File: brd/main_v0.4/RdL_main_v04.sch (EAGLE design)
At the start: 22 parts, among them J1 Test, J2 MPU

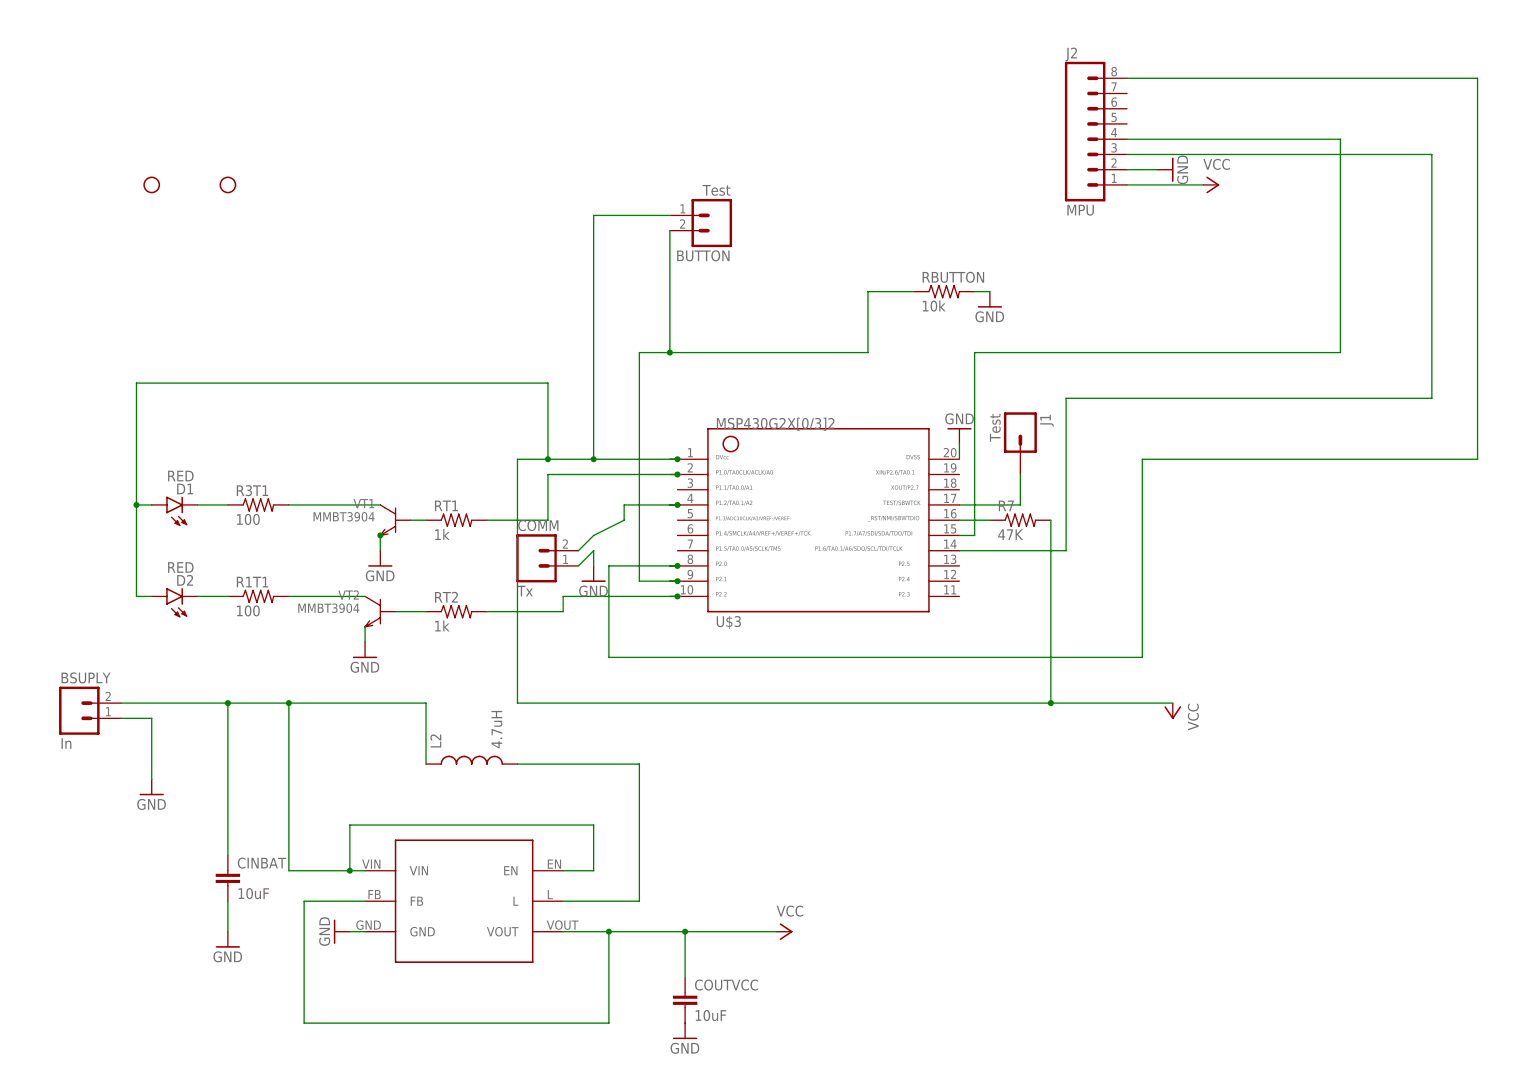
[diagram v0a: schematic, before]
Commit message: Added version 4 to divide in 3 boards
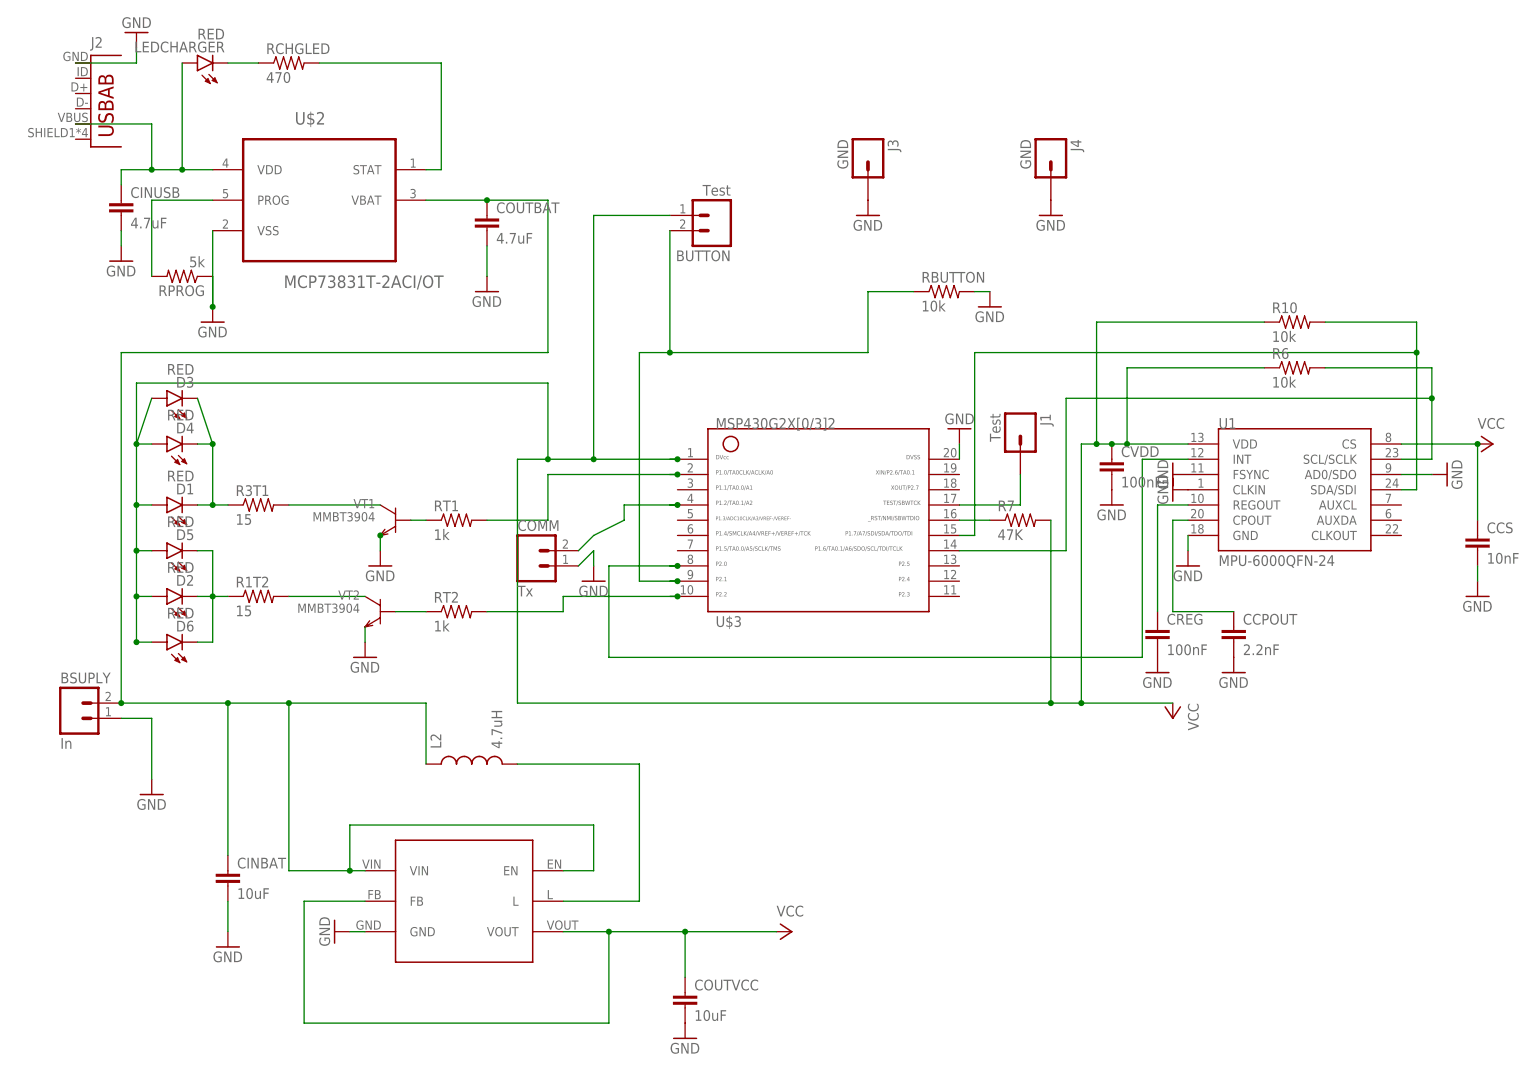
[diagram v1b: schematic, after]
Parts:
- removed H1, H3: STAND-OFF, SparkFun-Electromechanical:STAND-OFF
- added CCPOUT: 2.2nF, SparkFun-Capacitors:CAP0805
- added CCS: 10nF, SparkFun-Capacitors:CAP0805
- added CINUSB, COUTBAT: 4.7uF, SparkFun-Capacitors:CAP0805
- added CREG, CVDD: 100nF, SparkFun-Capacitors:CAP0805
- added D3, D4, D5, D6, LEDCHARGER: RED, SparkFun-LED:LED-RED1206
- added J3, J4: GND, SparkFun-Connectors:M01PTH
- added R10, R6: 10k, SparkFun-Resistors:RESISTOR0805-RES
- added RCHGLED: 470, SparkFun-Resistors:RESISTOR1206
- added RPROG: 5k, SparkFun-Resistors:RESISTOR1206
- added U$2: MCP73831T-2ACI/OT, MCP73831T-2ACI_OT:MCP73831T-2ACI/OT
- added U1: MPU-6000QFN-24, SparkFun-Sensors:MPU-6000QFN-24
- J2: value MPU -> (none); device SparkFun-Connectors:M08NO_SILK -> SparkFun-Connectors:USB-AB
- R1T2, R3T1: value 100 -> 15
- renumbered R1T1 to R1T2
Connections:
- removed net N$2: BSUPLY.2, CINBAT.1, L2.1, U$1.EN, U$1.VIN
- new net N$16: LEDCHARGER.C, RCHGLED.1
- new net N$19: RPROG.2, U$2.PROG
- new net N$23: CREG.1, U1.REGOUT
- new net N$26: CCPOUT.1, U1.CPOUT
- new net N$5: CINUSB.1, J2.VBUS, LEDCHARGER.A, U$2.VDD
- new net VINUSB: RCHGLED.2, U$2.STAT
- new net VOUTBATT: BSUPLY.2, CINBAT.1, COUTBAT.1, L2.1, U$1.EN, U$1.VIN, U$2.VBAT
- net GND: now also CCPOUT.2, CCS.2, CINUSB.2, COUTBAT.2, CREG.2, CVDD.2, J2.GND, J3.1, J4.1, RPROG.1, U$2.VSS, U1.AD0/SDO, U1.CLKIN, U1.FSYNC, U1.GND; no longer J2.2
- net N$13: now also D5.C, D6.C
- net N$14: now also D3.C, D4.C
- net N$18: now also U1.INT; no longer J2.8
- net N$20: now also R10.2, U1.SDA/SDI; no longer J2.4
- net N$22: now also R6.2, U1.SCL/SCLK; no longer J2.3
- net VCC: now also CCS.1, CVDD.1, D3.A, D4.A, D5.A, D6.A, R10.1, R6.1, U1.CS, U1.VDD; no longer J2.1

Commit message: Update main v4, almost ready for printing
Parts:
- added J10, J7, J8, J9: VCC, SparkFun-Connectors:M01PTH
- added J5, J6: GND, SparkFun-Connectors:M01PTH
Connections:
- net GND: now also J5.1, J6.1
- net VCC: now also J10.1, J7.1, J8.1, J9.1
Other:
- moved on the sheet: J4
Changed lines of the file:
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@@
 <part name="GND22" library="supply1" deviceset="GND" device=""/>
 <part name="GND23" library="supply1" deviceset="GND" device=""/>
+<part name="J5" library="SparkFun-Connectors" deviceset="M01" device="PTH" value="GND"/>
+<part name="GND24" library="supply1" deviceset="GND" device=""/>
+<part name="J6" library="SparkFun-Connectors" deviceset="M01" device="PTH" value="GND"/>
+<part name="GND25" library="supply1" deviceset="GND" device=""/>
+<part name="J7" library="SparkFun-Connectors" deviceset="M01" device="PTH" value="VCC"/>
+<part name="J8" library="SparkFun-Connectors" deviceset="M01" device="PTH" value="VCC"/>
+<part name="J9" library="SparkFun-Connectors" deviceset="M01" device="PTH" value="VCC"/>
+<part name="J10" library="SparkFun-Connectors" deviceset="M01" device="PTH" value="VCC"/>
+<part name="P+4" library="supply1" deviceset="VCC" device=""/>
+<part name="P+5" library="supply1" deviceset="VCC" device=""/>
+<part name="P+6" library="supply1" deviceset="VCC" device=""/>
+<part name="P+7" library="supply1" deviceset="VCC" device=""/>
 </parts>
 <sheets>
@@
 <instance part="D6" gate="G$1" x="0" y="73.66" rot="R90"/>
 <instance part="J3" gate="G$1" x="116.84" y="154.94" rot="R270"/>
-<instance part="J4" gate="G$1" x="147.32" y="154.94" rot="R270"/>
+<instance part="J4" gate="G$1" x="127" y="154.94" rot="R270"/>
 <instance part="GND22" gate="1" x="116.84" y="144.78"/>
-<instance part="GND23" gate="1" x="147.32" y="144.78"/>
+<instance part="GND23" gate="1" x="127" y="144.78"/>
+<instance part="J5" gate="G$1" x="76.2" y="170.18" rot="R270"/>
+<instance part="GND24" gate="1" x="76.2" y="160.02"/>
+<instance part="J6" gate="G$1" x="86.36" y="170.18" rot="R270"/>
+<instance part="GND25" gate="1" x="86.36" y="160.02"/>
+<instance part="J7" gate="G$1" x="149.86" y="165.1" rot="R270"/>
+<instance part="J8" gate="G$1" x="162.56" y="165.1" rot="R270"/>
+<instance part="J9" gate="G$1" x="177.8" y="165.1" rot="R270"/>
+<instance part="J10" gate="G$1" x="193.04" y="165.1" rot="R270"/>
+<instance part="P+4" gate="VCC" x="149.86" y="154.94" rot="R180"/>
+<instance part="P+5" gate="VCC" x="162.56" y="154.94" rot="R180"/>
+<instance part="P+6" gate="VCC" x="177.8" y="154.94" rot="R180"/>
+<instance part="P+7" gate="VCC" x="193.04" y="154.94" rot="R180"/>
 </instances>
 <busses>
@@
 <pinref part="J4" gate="G$1" pin="1"/>
 <pinref part="GND23" gate="1" pin="GND"/>
+</segment>
+<segment>
+<pinref part="J5" gate="G$1" pin="1"/>
+<pinref part="GND24" gate="1" pin="GND"/>
+</segment>
+<segment>
+<pinref part="J6" gate="G$1" pin="1"/>
+<pinref part="GND25" gate="1" pin="GND"/>
 </segment>
 </net>
@@
 <junction x="86.36" y="25.4"/>
 </segment>
-</net>
+<segment>
+<pinref part="J7" gate="G$1" pin="1"/>
+<pinref part="P+4" gate="VCC" pin="VCC"/>
+</segment>
+<segment>
+<pinref part="J8" gate="G$1" pin="1"/>
+<pinref part="P+5" gate="VCC" pin="VCC"/>
+</segment>
+<segment>
+<pinref part="J9" gate="G$1" pin="1"/>
+<pinref part="P+6" gate="VCC" pin="VCC"/>
+</segment>
+<segment>
+<pinref part="J10" gate="G$1" pin="1"/>
+<pinref part="P+7" gate="VCC" pin="VCC"/>
+</segment>
+</net>

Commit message: Version 4 without unrouted vias
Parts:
- added BSUPLY1: In, SparkFun-Connectors:M02PTH
- added J11, J12, J13, J14: LEDS1, SparkFun-Connectors:M01PTH
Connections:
- net GND: now also BSUPLY1.1
- net N$13: now also J13.1, J14.1
- net N$14: now also J11.1, J12.1
- net VOUTBATT: now also BSUPLY1.2
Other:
- moved on the sheet: R1T2, R3T1
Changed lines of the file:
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@@
 <part name="P+6" library="supply1" deviceset="VCC" device=""/>
 <part name="P+7" library="supply1" deviceset="VCC" device=""/>
+<part name="BSUPLY1" library="SparkFun-Connectors" deviceset="M02" device="PTH" value="In"/>
+<part name="GND26" library="supply1" deviceset="GND" device=""/>
+<part name="J11" library="SparkFun-Connectors" deviceset="M01" device="PTH" value="LEDS1"/>
+<part name="J12" library="SparkFun-Connectors" deviceset="M01" device="PTH" value="LEDS1"/>
+<part name="J13" library="SparkFun-Connectors" deviceset="M01" device="PTH" value="LEDS1"/>
+<part name="J14" library="SparkFun-Connectors" deviceset="M01" device="PTH" value="LEDS1"/>
 </parts>
 <sheets>
@@
 <instance part="CINUSB" gate="G$1" x="-7.62" y="144.78"/>
 <instance part="COUTBAT" gate="G$1" x="53.34" y="142.24"/>
-<instance part="R3T1" gate="G$1" x="15.24" y="96.52"/>
-<instance part="R1T2" gate="G$1" x="15.24" y="81.28"/>
+<instance part="R3T1" gate="G$1" x="25.4" y="96.52"/>
+<instance part="R1T2" gate="G$1" x="25.4" y="81.28"/>
 <instance part="L2" gate="G$1" x="50.8" y="53.34" rot="R90"/>
 <instance part="RPROG" gate="G$1" x="2.54" y="134.62" rot="R180"/>
@@
 <instance part="P+6" gate="VCC" x="177.8" y="154.94" rot="R180"/>
 <instance part="P+7" gate="VCC" x="193.04" y="154.94" rot="R180"/>
+<instance part="BSUPLY1" gate="G$1" x="-12.7" y="30.48"/>
+<instance part="GND26" gate="1" x="-2.54" y="25.4" rot="R90"/>
+<instance part="J11" gate="G$1" x="12.7" y="111.76" rot="R270"/>
+<instance part="J12" gate="G$1" x="22.86" y="111.76" rot="R270"/>
+<instance part="J13" gate="G$1" x="10.16" y="68.58" rot="R90"/>
+<instance part="J14" gate="G$1" x="17.78" y="68.58" rot="R90"/>
 </instances>
 <busses>
@@
 <pinref part="GND25" gate="1" pin="GND"/>
 </segment>
+<segment>
+<pinref part="BSUPLY1" gate="G$1" pin="1"/>
+<pinref part="GND26" gate="1" pin="GND"/>
+<wire x1="-5.08" y1="30.48" x2="-5.08" y2="25.4" width="0.1524" layer="91"/>
+</segment>
 </net>
 <net name="N$6" class="0">
 <segment>
 <pinref part="VT2" gate="G$1" pin="C"/>
-<wire x1="20.32" y1="81.28" x2="33.02" y2="81.28" width="0.1524" layer="91"/>
+<wire x1="30.48" y1="81.28" x2="33.02" y2="81.28" width="0.1524" layer="91"/>
 <pinref part="R1T2" gate="G$1" pin="2"/>
 </segment>
@@
 <segment>
 <pinref part="VT1" gate="G$1" pin="C"/>
-<wire x1="20.32" y1="96.52" x2="35.56" y2="96.52" width="0.1524" layer="91"/>
+<wire x1="30.48" y1="96.52" x2="35.56" y2="96.52" width="0.1524" layer="91"/>
 <pinref part="R3T1" gate="G$1" pin="2"/>
 </segment>
@@
 <net name="N$13" class="0">
 <segment>
-<wire x1="10.16" y1="81.28" x2="7.62" y2="81.28" width="0.1524" layer="91"/>
+<wire x1="20.32" y1="81.28" x2="12.7" y2="81.28" width="0.1524" layer="91"/>
 <pinref part="D2" gate="G$1" pin="C"/>
 <pinref part="R1T2" gate="G$1" pin="1"/>
 <pinref part="D5" gate="G$1" pin="C"/>
+<wire x1="12.7" y1="81.28" x2="7.62" y2="81.28" width="0.1524" layer="91"/>
 <wire x1="7.62" y1="81.28" x2="5.08" y2="81.28" width="0.1524" layer="91"/>
 <wire x1="5.08" y1="88.9" x2="7.62" y2="88.9" width="0.1524" layer="91"/>
@@
 <wire x1="7.62" y1="73.66" x2="7.62" y2="81.28" width="0.1524" layer="91"/>
 <junction x="7.62" y="81.28"/>
+<pinref part="J13" gate="G$1" pin="1"/>
+<wire x1="10.16" y1="76.2" x2="12.7" y2="81.28" width="0.1524" layer="91"/>
+<junction x="12.7" y="81.28"/>
+<pinref part="J14" gate="G$1" pin="1"/>
+<wire x1="17.78" y1="76.2" x2="20.32" y2="81.28" width="0.1524" layer="91"/>
+<junction x="20.32" y="81.28"/>
 </segment>
 </net>
 <net name="N$14" class="0">
 <segment>
-<wire x1="10.16" y1="96.52" x2="7.62" y2="96.52" width="0.1524" layer="91"/>
+<wire x1="20.32" y1="96.52" x2="17.78" y2="96.52" width="0.1524" layer="91"/>
 <pinref part="D1" gate="G$1" pin="C"/>
 <pinref part="R3T1" gate="G$1" pin="1"/>
 <pinref part="D3" gate="G$1" pin="C"/>
+<wire x1="17.78" y1="96.52" x2="12.7" y2="96.52" width="0.1524" layer="91"/>
+<wire x1="12.7" y1="96.52" x2="7.62" y2="96.52" width="0.1524" layer="91"/>
 <wire x1="7.62" y1="96.52" x2="5.08" y2="96.52" width="0.1524" layer="91"/>
 <wire x1="5.08" y1="114.3" x2="7.62" y2="106.68" width="0.1524" layer="91"/>
@@
 <wire x1="5.08" y1="106.68" x2="7.62" y2="106.68" width="0.1524" layer="91"/>
 <junction x="7.62" y="106.68"/>
+<pinref part="J11" gate="G$1" pin="1"/>
+<wire x1="12.7" y1="104.14" x2="12.7" y2="96.52" width="0.1524" layer="91"/>
+<junction x="12.7" y="96.52"/>
+<pinref part="J12" gate="G$1" pin="1"/>
+<wire x1="22.86" y1="104.14" x2="17.78" y2="96.52" width="0.1524" layer="91"/>
+<junction x="17.78" y="96.52"/>
 </segment>
 </net>
@@
 <segment>
 <pinref part="BSUPLY" gate="G$1" pin="2"/>
-<wire x1="-7.62" y1="63.5" x2="10.16" y2="63.5" width="0.1524" layer="91"/>
+<wire x1="-7.62" y1="63.5" x2="2.54" y2="63.5" width="0.1524" layer="91"/>
+<wire x1="2.54" y1="63.5" x2="10.16" y2="63.5" width="0.1524" layer="91"/>
 <wire x1="10.16" y1="63.5" x2="20.32" y2="63.5" width="0.1524" layer="91"/>
 <wire x1="20.32" y1="63.5" x2="20.32" y2="35.56" width="0.1524" layer="91"/>
@@
 <junction x="53.34" y="147.32"/>
 <junction x="20.32" y="63.5"/>
-</segment>
-</net>
+<pinref part="BSUPLY1" gate="G$1" pin="2"/>
+<wire x1="-5.08" y1="33.02" x2="2.54" y2="27.94" width="0.1524" layer="91"/>
+<wire x1="2.54" y1="27.94" x2="2.54" y2="63.5" width="0.1524" layer="91"/>
+<junction x="2.54" y="63.5"/>
+</segment>
+</net>
